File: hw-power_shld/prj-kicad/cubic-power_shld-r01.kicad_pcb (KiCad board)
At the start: 2 copper layers, 13.3 x 24.5 mm, 17 parts

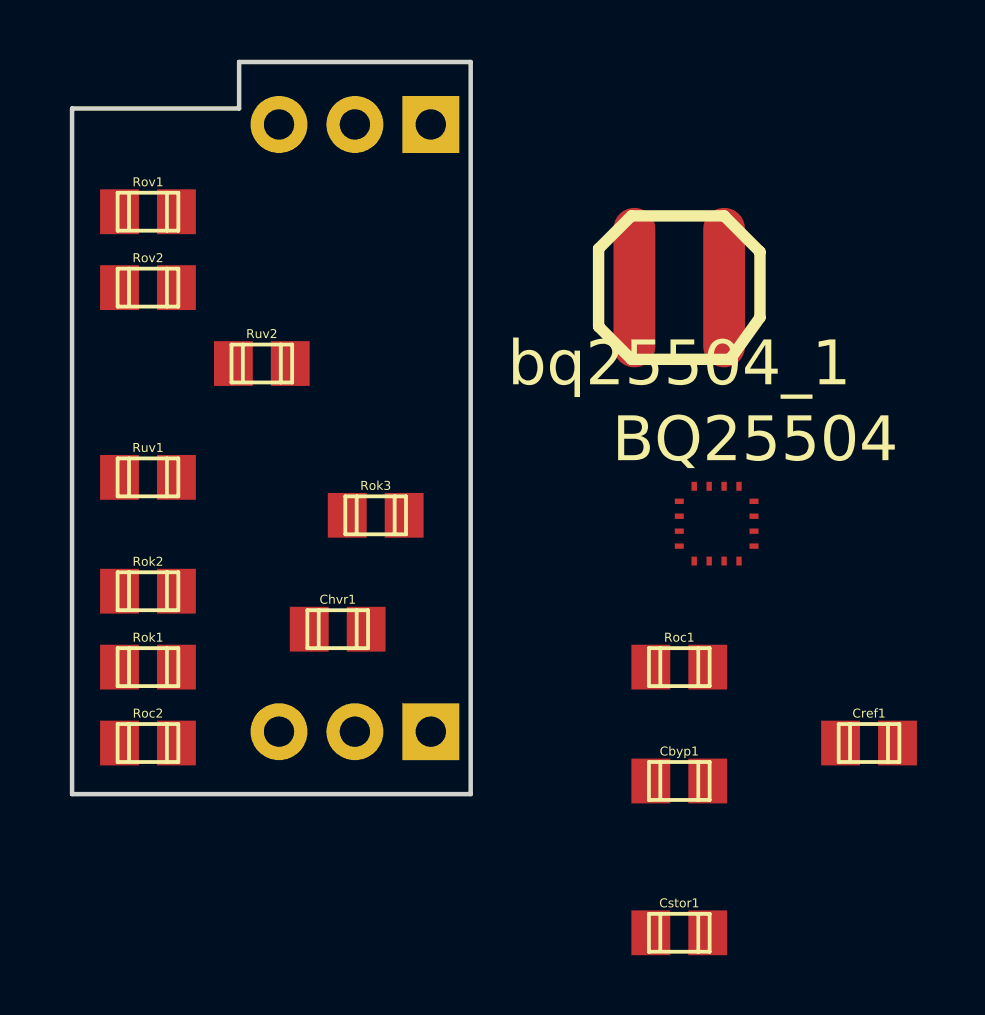
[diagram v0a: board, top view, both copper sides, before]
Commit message: correction erreur symbole masse placement des composants
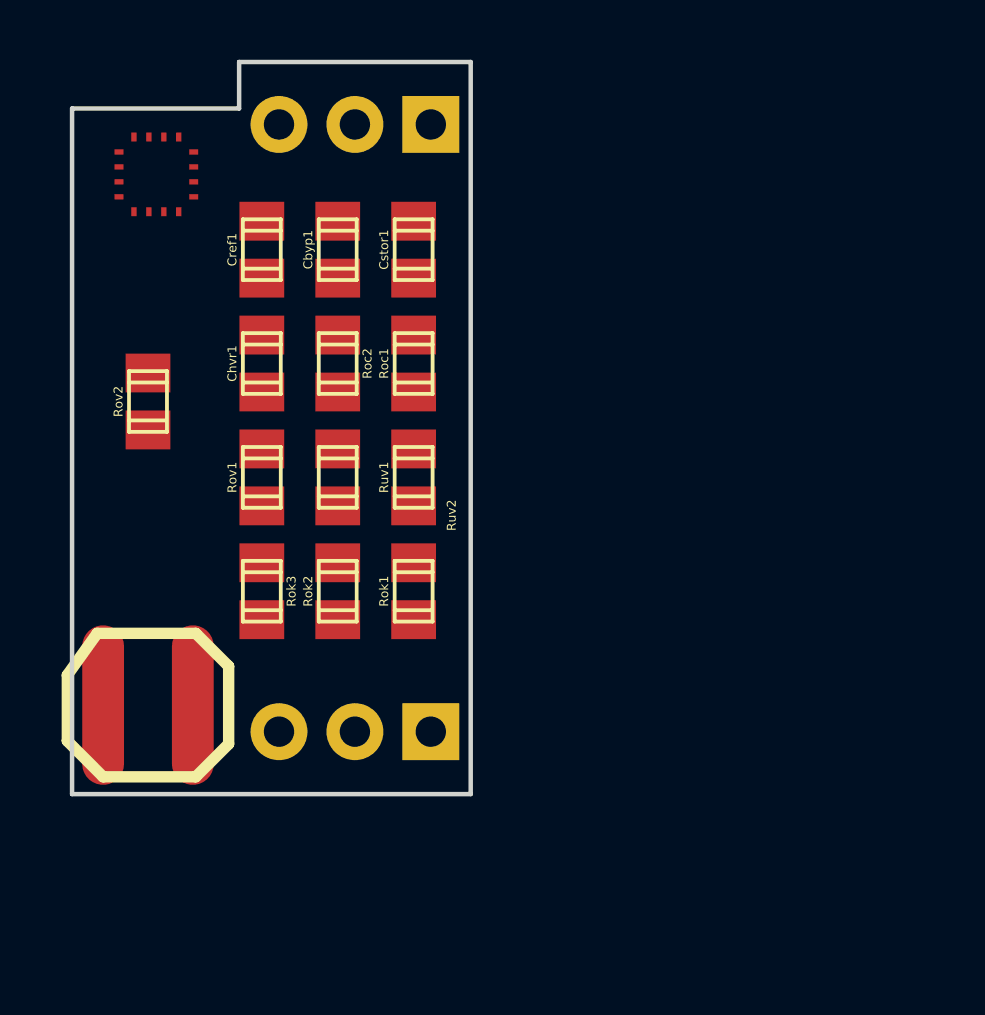
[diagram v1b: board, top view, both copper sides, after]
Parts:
- removed Lbst1: INDUCTOR, LPS4018
- removed bq25504_1: BQ25504, RGT_S-PVQFN-N16
- added ?: , RGT_S-PVQFN-N16, F.Cu at (170.2, 80.0)
- added ?: , LPS4018, F.Cu at (171.4, 96.5)
- moved Cref1 26.2 mm to (175.3, 81.3), turned to 90 degrees
- moved Cstor1 24.5 mm to (180.3, 81.3), turned to 90 degrees
- moved Cbyp1 21.1 mm to (177.8, 81.3), turned to 90 degrees
- moved Roc2 14.2 mm to (177.8, 85.1), turned to 270 degrees
- moved Roc1 13.5 mm to (180.3, 85.1), turned to 90 degrees
- moved Rov1 9.67 mm to (175.3, 88.9), turned to 90 degrees
- moved Rok1 9.25 mm to (180.3, 92.7), turned to 90 degrees
- moved Chvr1 9.25 mm to (175.3, 85.1), turned to 90 degrees
- moved Ruv1 8.89 mm to (180.3, 88.9), turned to 90 degrees
- moved Rok2 6.35 mm to (177.8, 92.7), turned to 90 degrees
- moved Ruv2 4.58 mm to (177.8, 88.9), turned to 270 degrees
- moved Rok3 4.58 mm to (175.3, 92.7), turned to 270 degrees
- moved Rov2 3.81 mm to (171.4, 86.4), turned to 90 degrees
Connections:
- Chvr1 pad 1: N-000008 -> GND
- Cref1 pad 2: N-0000011 -> GND
- PWR_OUT1 pad 6: N-000008 -> GND
- Roc1 pad 2: N-000008 -> GND
- Rok1 pad 2: (no net) -> GND
- Rov1 pad 2: N-000007 (its old number) -> GND
- Ruv1 pad 2: N-000007 (its old number) -> GND

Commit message: gnd done
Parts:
- moved ? 11.4 mm to (170.2, 91.4)
- turned Rov2 to 0 degrees
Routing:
- net GND: track 0.00 -> 37.5 mm
- net N-0000012: track 0.00 -> 8.50 mm
- net N-0000015: track 0.00 -> 5.79 mm
- net N-000008: track 0.00 -> 5.51 mm
- net N-000006: track 0.00 -> 3.02 mm
- net N-000001: track 0.00 -> 2.99 mm
- net N-000004: track 0.00 -> 2.54 mm
- net N-000007: track 0.00 -> 2.54 mm
- net N-000005: track 0.00 -> 2.54 mm
- net N-000003: track 0.00 -> 2.54 mm
- net N-000002: track 0.00 -> 2.54 mm
- net N-0000013: track 0.00 -> 2.54 mm
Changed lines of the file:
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@@
   (general
     (links 35)
-    (no_connects 35)
-    (area 140.97 66.04 181.61 106.68)
+    (no_connects 12)
+    (area 142.174999 67.174999 182.414439 107.325001)
     (thickness 1.6)
     (drawings 20)
-    (tracks 0)
+    (tracks 50)
     (zones 0)
     (modules 17)
@@
   )
   (module RGT_S-PVQFN-N16   placed (layer F.Cu)
-    (at 170.18 80.01 90)
+    (at 170.18 91.44 90)
     (fp_text reference "" (at 0 -3.81 90) (layer F.SilkS)
       (effects (font (size 1.5 1.5) (thickness 0.15)))
@@
   )
   (module c_0805 (layer F.Cu)
-    (at 171.45 86.36 90)
-    (descr "SMT capacitor, 0805")
-    (fp_text reference Rov2 (at 0 -0.9906 90) (layer F.SilkS)
-      (effects (font (size 0.29972 0.29972) (thickness 0.06096)))
-    )
-    (fp_text value R (at 0 0.9906 90) (layer F.SilkS) hide
-      (effects (font (size 0.29972 0.29972) (thickness 0.06096)))
-    )
-    (fp_line (start 0.635 -0.635) (end 0.635 0.635) (layer F.SilkS) (width 0.127))
-    (fp_line (start -0.635 -0.635) (end -0.635 0.6096) (layer F.SilkS) (width 0.127))
-    (fp_line (start -1.016 -0.635) (end 1.016 -0.635) (layer F.SilkS) (width 0.127))
-    (fp_line (start 1.016 -0.635) (end 1.016 0.635) (layer F.SilkS) (width 0.127))
-    (fp_line (start 1.016 0.635) (end -1.016 0.635) (layer F.SilkS) (width 0.127))
-    (fp_line (start -1.016 0.635) (end -1.016 -0.635) (layer F.SilkS) (width 0.127))
-    (pad 1 smd rect (at 0.9525 0 90) (size 1.30048 1.4986)
+    (at 171.45 86.36)
+    (descr "SMT capacitor, 0805")
+    (fp_text reference Rov2 (at 0 -0.9906) (layer F.SilkS)
+      (effects (font (size 0.29972 0.29972) (thickness 0.06096)))
+    )
+    (fp_text value R (at 0 0.9906) (layer F.SilkS) hide
+      (effects (font (size 0.29972 0.29972) (thickness 0.06096)))
+    )
+    (fp_line (start 0.635 -0.635) (end 0.635 0.635) (layer F.SilkS) (width 0.127))
+    (fp_line (start -0.635 -0.635) (end -0.635 0.6096) (layer F.SilkS) (width 0.127))
+    (fp_line (start -1.016 -0.635) (end 1.016 -0.635) (layer F.SilkS) (width 0.127))
+    (fp_line (start 1.016 -0.635) (end 1.016 0.635) (layer F.SilkS) (width 0.127))
+    (fp_line (start 1.016 0.635) (end -1.016 0.635) (layer F.SilkS) (width 0.127))
+    (fp_line (start -1.016 0.635) (end -1.016 -0.635) (layer F.SilkS) (width 0.127))
+    (pad 1 smd rect (at 0.9525 0) (size 1.30048 1.4986)
       (layers F.Cu F.Paste F.Mask)
       (net 11 N-000006)
     )
-    (pad 2 smd rect (at -0.9525 0 90) (size 1.30048 1.4986)
+    (pad 2 smd rect (at -0.9525 0) (size 1.30048 1.4986)
       (layers F.Cu F.Paste F.Mask)
       (net 2 N-000001)
@@
   (gr_line (start 142.25 75) (end 150 75) (angle 90) (layer Dwgs.User) (width 0.15))
   (gr_line (start 142.25 75) (end 142.25 99.5) (angle 90) (layer Dwgs.User) (width 0.15))
+  (segment (start 170.98 88.94) (end 170.98 89.7) (width 0.254) (layer F.Cu) (net 1))
+  (segment (start 172.22 90.94) (end 172.98 90.94) (width 0.254) (layer F.Cu) (net 1))
+  (segment (start 170.98 89.7) (end 172.22 90.94) (width 0.254) (layer F.Cu) (net 1))
+  (segment (start 170.48 90.94) (end 172.98 90.94) (width 0.254) (layer F.Cu) (net 1))
+  (segment (start 172.48 91.44) (end 172.98 90.94) (width 0.254) (layer F.Cu) (net 1))
+  (segment (start 172.98 90.94) (end 174.1725 90.94) (width 0.254) (layer F.Cu) (net 1))
+  (segment (start 174.1725 90.94) (end 175.26 89.8525) (width 0.254) (layer F.Cu) (net 1))
+  (segment (start 175.26 84.1375) (end 175.5775 84.1375) (width 0.254) (layer F.Cu) (net 1))
+  (segment (start 179.3875 85.09) (end 180.34 86.0425) (width 0.254) (layer F.Cu) (net 1))
+  (segment (start 176.53 85.09) (end 179.3875 85.09) (width 0.254) (layer F.Cu) (net 1))
+  (segment (start 175.5775 84.1375) (end 176.53 85.09) (width 0.254) (layer F.Cu) (net 1))
+  (segment (start 175.26 89.8525) (end 175.5775 89.8525) (width 0.254) (layer F.Cu) (net 1))
+  (segment (start 179.3875 88.9) (end 180.34 89.8525) (width 0.254) (layer F.Cu) (net 1))
+  (segment (start 176.53 88.9) (end 179.3875 88.9) (width 0.254) (layer F.Cu) (net 1))
+  (segment (start 175.5775 89.8525) (end 176.53 88.9) (width 0.254) (layer F.Cu) (net 1))
+  (segment (start 175.26 84.1375) (end 175.26 82.2325) (width 0.254) (layer F.Cu) (net 1))
+  (segment (start 180.34 86.0425) (end 181.2925 86.0425) (width 0.254) (layer F.Cu) (net 1))
+  (segment (start 181.2925 86.0425) (end 181.61 86.36) (width 0.254) (layer F.Cu) (net 1))
+  (segment (start 181.61 86.36) (end 181.61 90.17) (width 0.254) (layer F.Cu) (net 1))
+  (segment (start 180.34 89.8525) (end 181.2925 89.8525) (width 0.254) (layer F.Cu) (net 1))
+  (segment (start 181.61 92.3925) (end 180.34 93.6625) (width 0.254) (layer F.Cu) (net 1))
+  (segment (start 181.61 90.17) (end 181.61 92.3925) (width 0.254) (layer F.Cu) (net 1))
+  (segment (start 181.2925 89.8525) (end 181.61 90.17) (width 0.254) (layer F.Cu) (net 1))
+  (segment (start 180.34 93.6625) (end 180.34 96.835) (width 0.254) (layer F.Cu) (net 1))
+  (segment (start 180.34 96.835) (end 180.915 97.41) (width 0.254) (layer F.Cu) (net 1))
+  (segment (start 170.4975 86.36) (end 170.4975 86.6775) (width 0.254) (layer F.Cu) (net 2))
+  (segment (start 171.48 88.87) (end 171.48 88.94) (width 0.254) (layer F.Cu) (net 2))
+  (segment (start 171.48 87.66) (end 171.48 88.87) (width 0.254) (layer F.Cu) (net 2))
+  (segment (start 170.4975 86.6775) (end 171.48 87.66) (width 0.254) (layer F.Cu) (net 2))
+  (segment (start 180.34 82.2325) (end 177.8 82.2325) (width 0.254) (layer F.Cu) (net 3))
+  (segment (start 180.915 77.09) (end 180.915 78.045) (width 0.254) (layer F.Cu) (net 3))
+  (segment (start 181.61 80.9625) (end 180.34 82.2325) (width 0.254) (layer F.Cu) (net 3))
+  (segment (start 181.61 78.74) (end 181.61 80.9625) (width 0.254) (layer F.Cu) (net 3))
+  (segment (start 180.915 78.045) (end 181.61 78.74) (width 0.254) (layer F.Cu) (net 3))
+  (segment (start 177.8 80.3275) (end 180.34 80.3275) (width 0.254) (layer F.Cu) (net 4))
+  (segment (start 177.8 86.0425) (end 175.26 86.0425) (width 0.254) (layer F.Cu) (net 6))
+  (segment (start 175.835 97.41) (end 173.84114 97.41) (width 0.254) (layer F.Cu) (net 6))
+  (segment (start 173.84114 97.41) (end 172.95114 96.52) (width 0.254) (layer F.Cu) (net 6))
+  (segment (start 175.835 77.09) (end 178.375 77.09) (width 0.254) (layer F.Cu) (net 7))
+  (segment (start 177.8 91.7575) (end 180.34 91.7575) (width 0.254) (layer F.Cu) (net 8))
+  (segment (start 175.26 93.6625) (end 177.8 93.6625) (width 0.254) (layer F.Cu) (net 9))
+  (segment (start 180.34 87.9475) (end 177.8 87.9475) (width 0.254) (layer F.Cu) (net 10))
+  (segment (start 172.72 87.63) (end 172.72 86.6775) (width 0.254) (layer F.Cu) (net 11))
+  (segment (start 171.98 88.37) (end 172.72 87.63) (width 0.254) (layer F.Cu) (net 11))
+  (segment (start 171.98 88.94) (end 171.98 88.37) (width 0.254) (layer F.Cu) (net 11))
+  (segment (start 172.72 86.6775) (end 172.4025 86.36) (width 0.254) (layer F.Cu) (net 11))
+  (segment (start 177.8 84.1375) (end 180.34 84.1375) (width 0.254) (layer F.Cu) (net 12))
+  (segment (start 170.98 91.44) (end 170.98 91.91) (width 0.254) (layer F.Cu) (net 13))
+  (segment (start 169.94886 92.94114) (end 169.94886 96.52) (width 0.254) (layer F.Cu) (net 13))
+  (segment (start 170.98 91.91) (end 169.94886 92.94114) (width 0.254) (layer F.Cu) (net 13))
 )

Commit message: routage fini
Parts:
- moved Rok2 12.5 mm to (172.7, 81.3)
- moved ? 11.4 mm to (178.3, 83.4), turned to 270 degrees
- moved Rok3 10.5 mm to (170.4, 83.4), turned to 90 degrees
- moved Ruv1 10.1 mm to (170.4, 87.1)
- moved Cref1 9.89 mm to (177.1, 91.0)
- moved Rok1 8.41 mm to (172.7, 89.2)
- moved Chvr1 8.35 mm to (181.2, 91.0), turned to 270 degrees
- moved Rov2 8.28 mm to (172.1, 78.1), turned to 180 degrees
- moved Ruv2 6.27 mm to (172.7, 85.2), turned to 90 degrees
- moved Roc1 6.02 mm to (179.2, 91.0)
- moved Roc2 2.57 mm to (180.3, 85.5), turned to 0 degrees
- moved Rov1 2.11 mm to (175.0, 91.0)
- moved Cbyp1 1.22 mm to (178.8, 80.5), turned to 270 degrees
- moved Cstor1 0.95 mm to (180.9, 80.5), turned to 270 degrees
- moved ? 0.78 mm to (171.9, 95.9), turned to 90 degrees
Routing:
- net N-000008: track 5.51 -> 27.3 mm, vias 0 -> 2
- net N-0000015: track 5.79 -> 27.1 mm, vias 0 -> 2
- net N-000001: track 2.99 -> 18.6 mm, vias 0 -> 2
- net N-000003: track 2.54 -> 17.8 mm, vias 0 -> 2
- net N-000006: track 3.02 -> 17.3 mm, vias 0 -> 2
- net N-000002: track 2.54 -> 9.28 mm
- net N-0000014: track 0.00 -> 5.21 mm
- net N-000004: track 2.54 -> 7.07 mm
- net N-0000012: track 8.50 -> 4.56 mm
- net N-000007: track 2.54 -> 6.08 mm
- net N-000005: track 2.54 -> 5.75 mm
- net N-0000013: track 2.54 -> 5.12 mm
- net GND: track 37.5 -> 40.0 mm, vias 0 -> 2

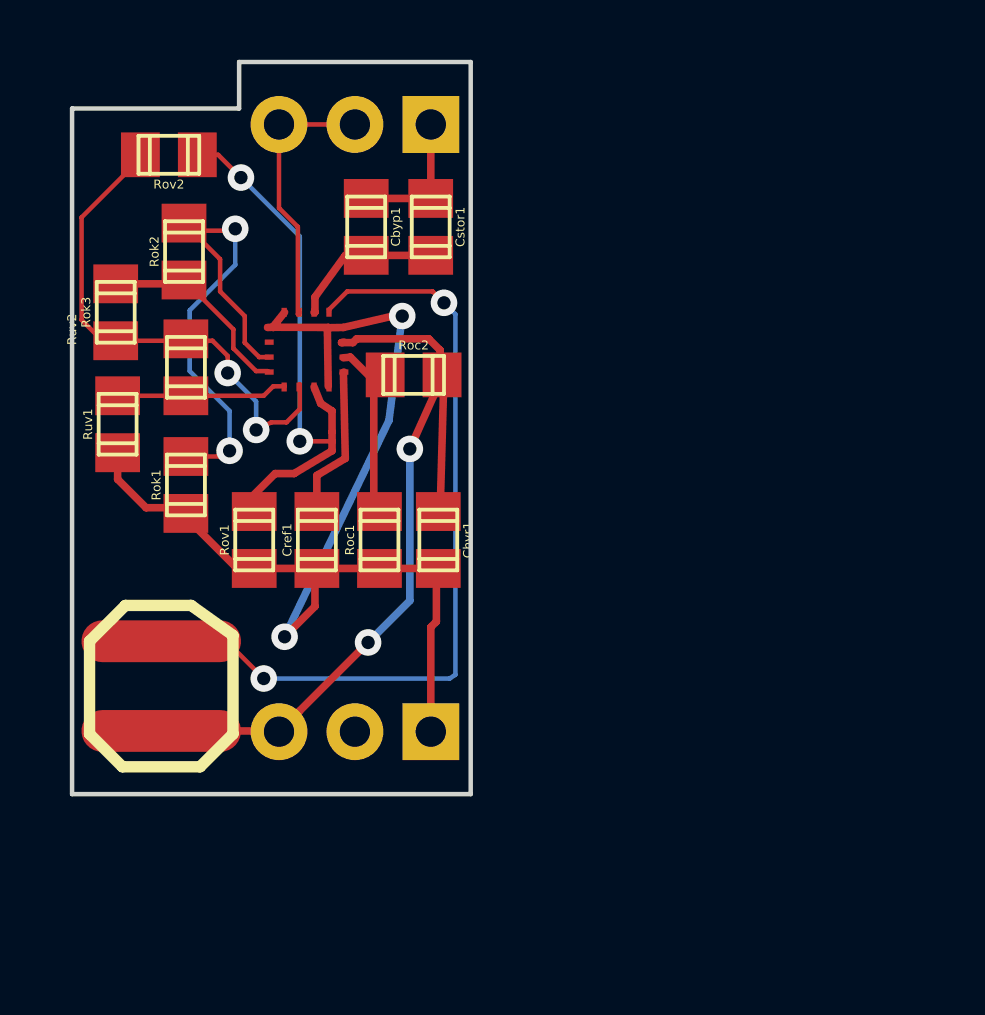
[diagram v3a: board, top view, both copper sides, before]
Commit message: route modifiées en fonction des infos de Hooli
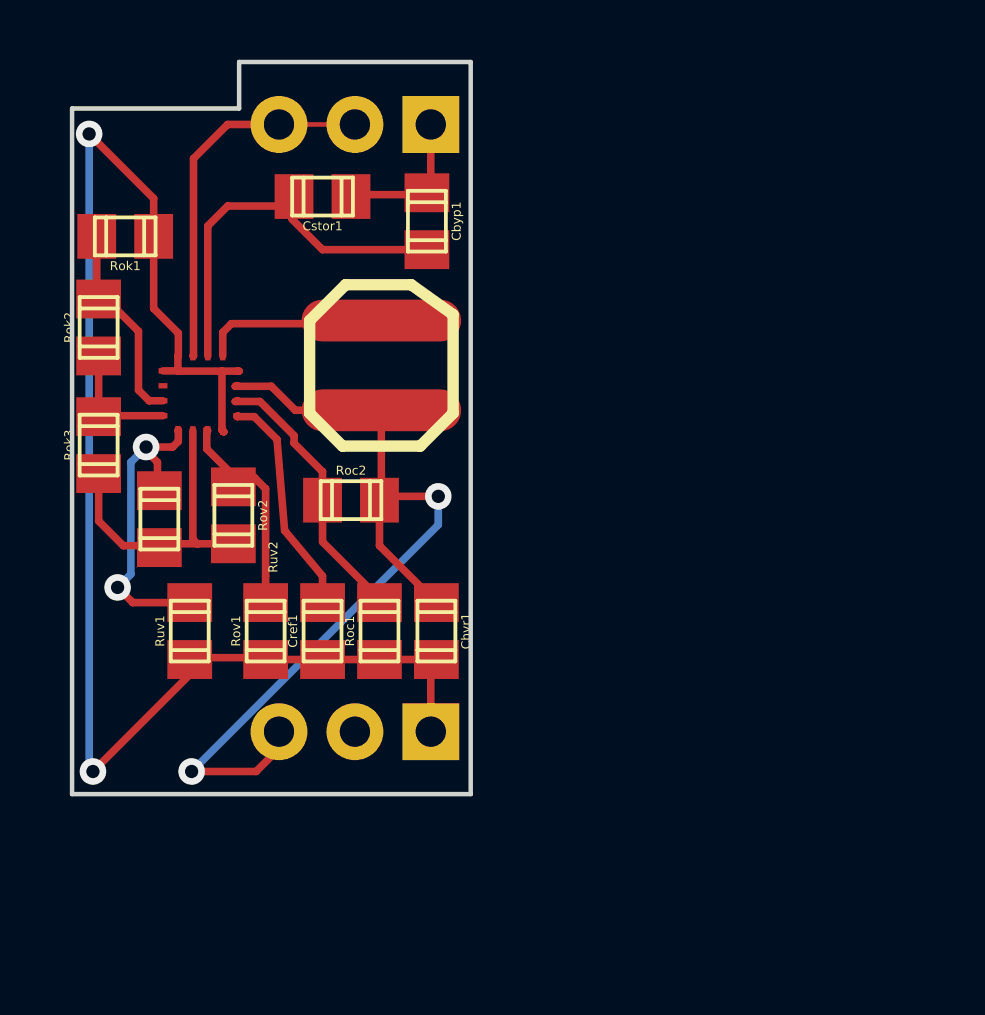
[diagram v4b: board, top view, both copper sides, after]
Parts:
- moved ? 13.0 mm to (179.3, 85.2)
- moved Rov2 12.3 mm to (174.3, 90.2), turned to 270 degrees
- moved Rok1 8.56 mm to (170.7, 80.8), turned to 180 degrees
- moved Ruv1 7.33 mm to (172.8, 94.0)
- moved Ruv2 5.16 mm to (171.8, 90.3), turned to 270 degrees
- moved Roc2 4.69 mm to (178.2, 89.7)
- moved Rok3 4.48 mm to (169.8, 87.8)
- moved ? 3.84 mm to (174.8, 84.8)
- moved Rok2 3.82 mm to (169.8, 83.9)
- moved Cstor1 3.76 mm to (177.3, 79.5), turned to 180 degrees
- moved Rov1 3.07 mm to (175.4, 94.0)
- moved Cref1 3.05 mm to (177.3, 94.0)
- moved Chvr1 3.05 mm to (181.1, 94.0)
- moved Roc1 3.05 mm to (179.2, 94.0)
- moved Cbyp1 2.04 mm to (180.8, 80.3)
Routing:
- net N-000008: track 27.3 -> 6.24 mm, vias 2 -> 0
- net N-000001: track 18.6 -> 7.01 mm, vias 2 -> 0
- net GND: track 40.0 -> 51.0 mm
- net N-000003: track 17.8 -> 6.82 mm, vias 2 -> 0
- net N-0000013: track 5.12 -> 13.3 mm
- net N-000006: track 17.3 -> 9.93 mm, vias 2 -> 0
- net N-000005: track 5.75 -> 10.9 mm, vias 0 -> 2
- net N-0000015: track 27.1 -> 31.1 mm
- net N-000007: track 6.08 -> 9.48 mm
- net N-000002: track 9.28 -> 12.6 mm
- net N-000004: track 7.07 -> 4.22 mm
- net N-0000014: track 5.21 -> 7.62 mm

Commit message: move some R move reference
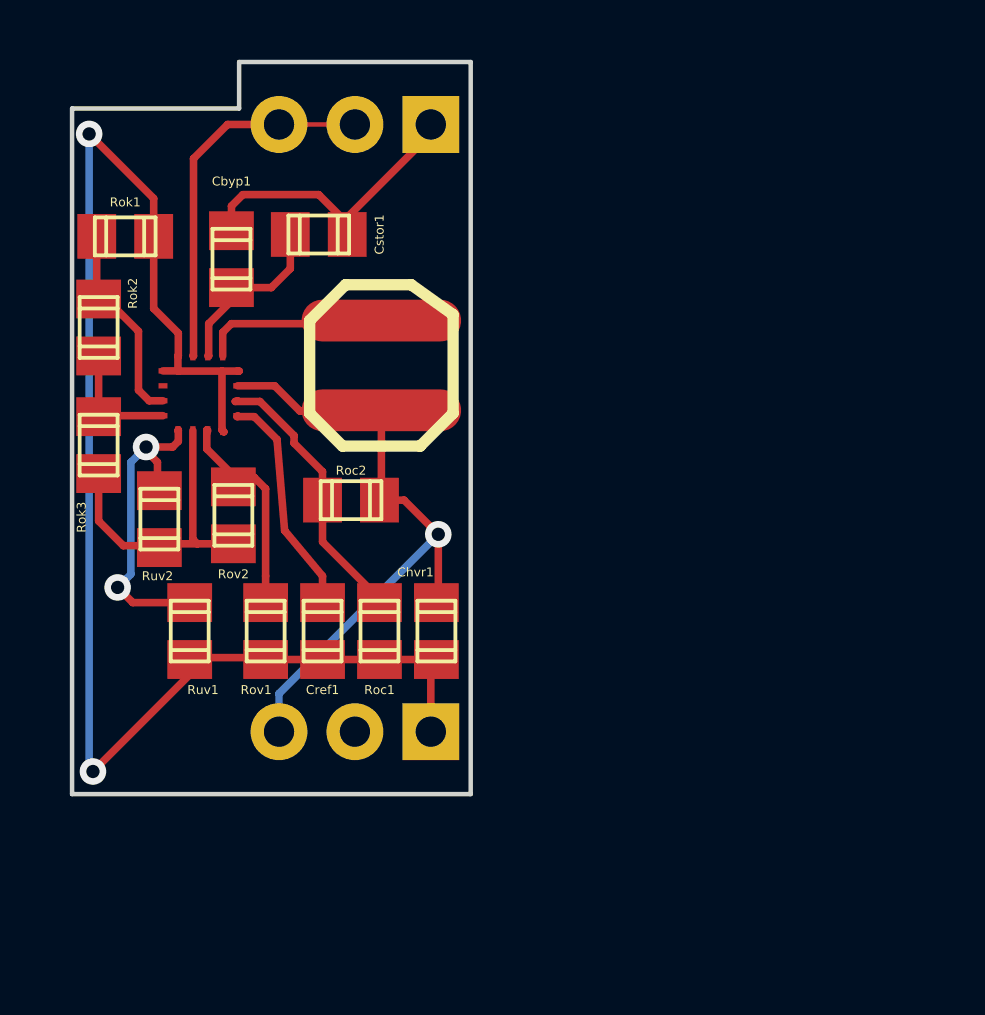
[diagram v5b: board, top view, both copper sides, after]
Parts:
- moved Cbyp1 6.66 mm to (174.2, 81.6)
- moved Cstor1 1.28 mm to (177.2, 80.8)
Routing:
- net N-0000015: track 31.1 -> 22.0 mm, vias 2 -> 1
- net N-0000013: track 13.3 -> 6.01 mm
- net N-0000012: track 5.04 -> 9.69 mm
